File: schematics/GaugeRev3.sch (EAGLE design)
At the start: 35 parts, among them U1 ARDUINO_MINI, U2 VID29, U3 FT232RL-BASICSSOP

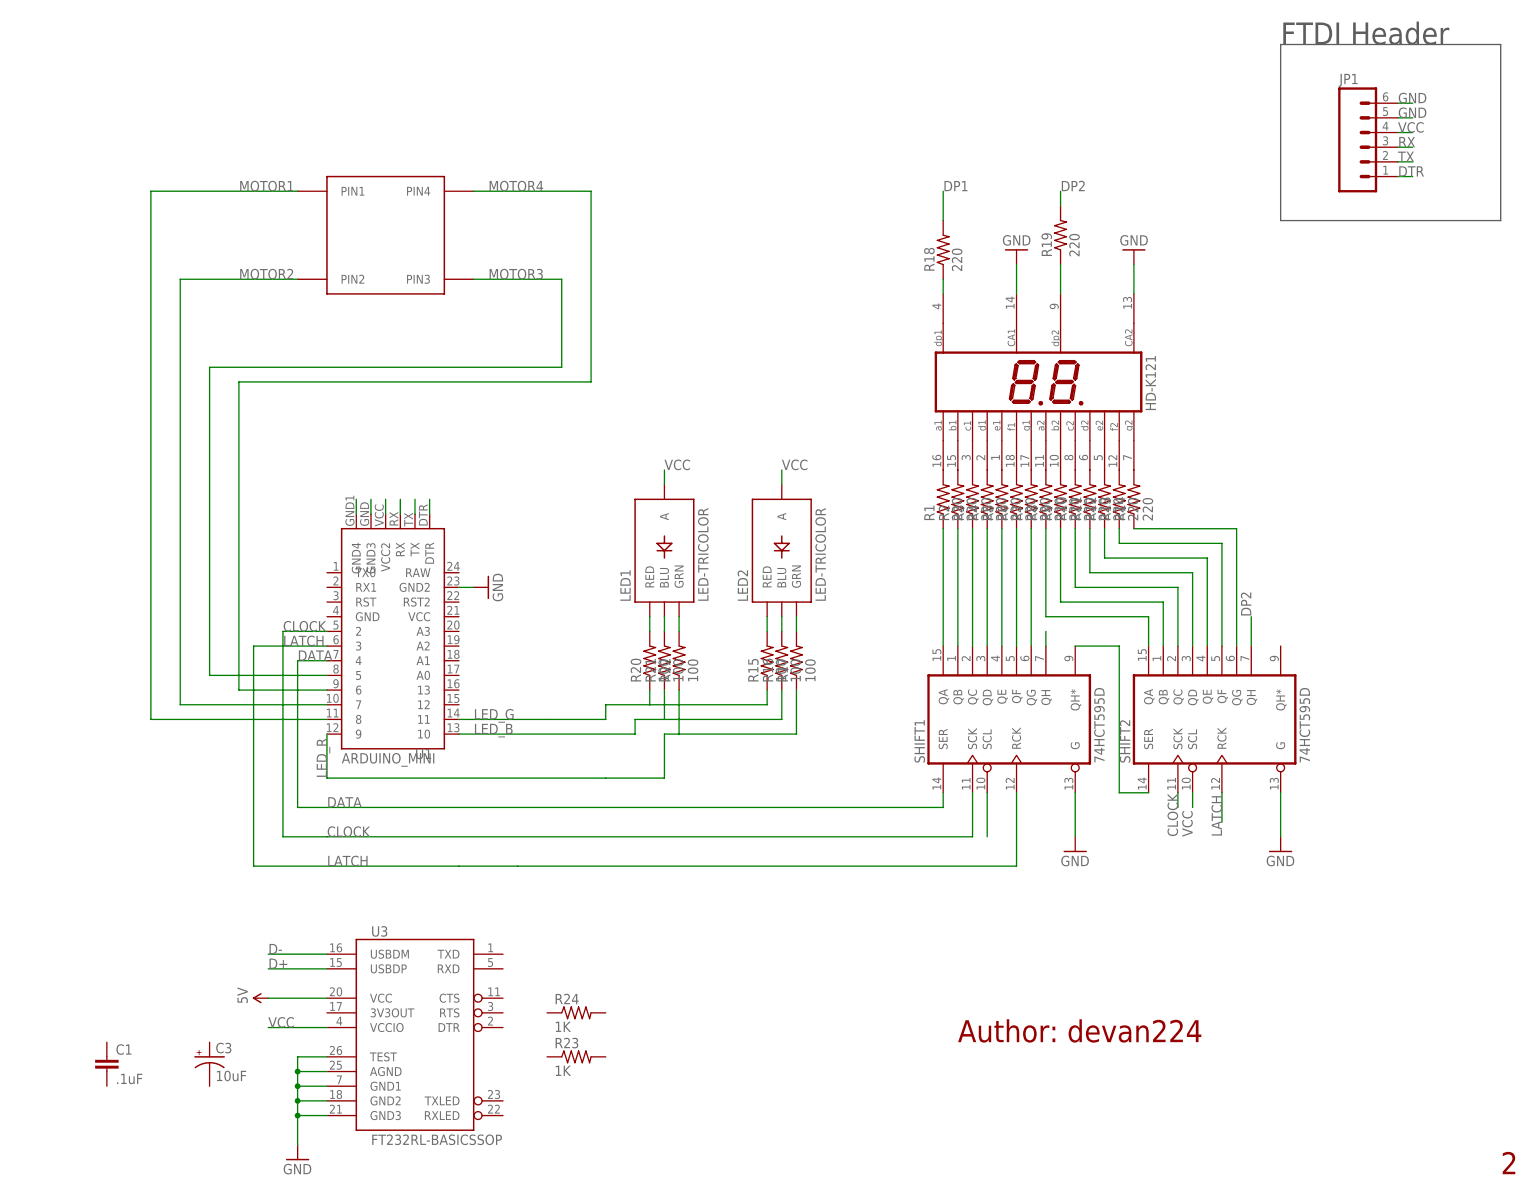
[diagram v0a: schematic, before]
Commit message: updated schematics
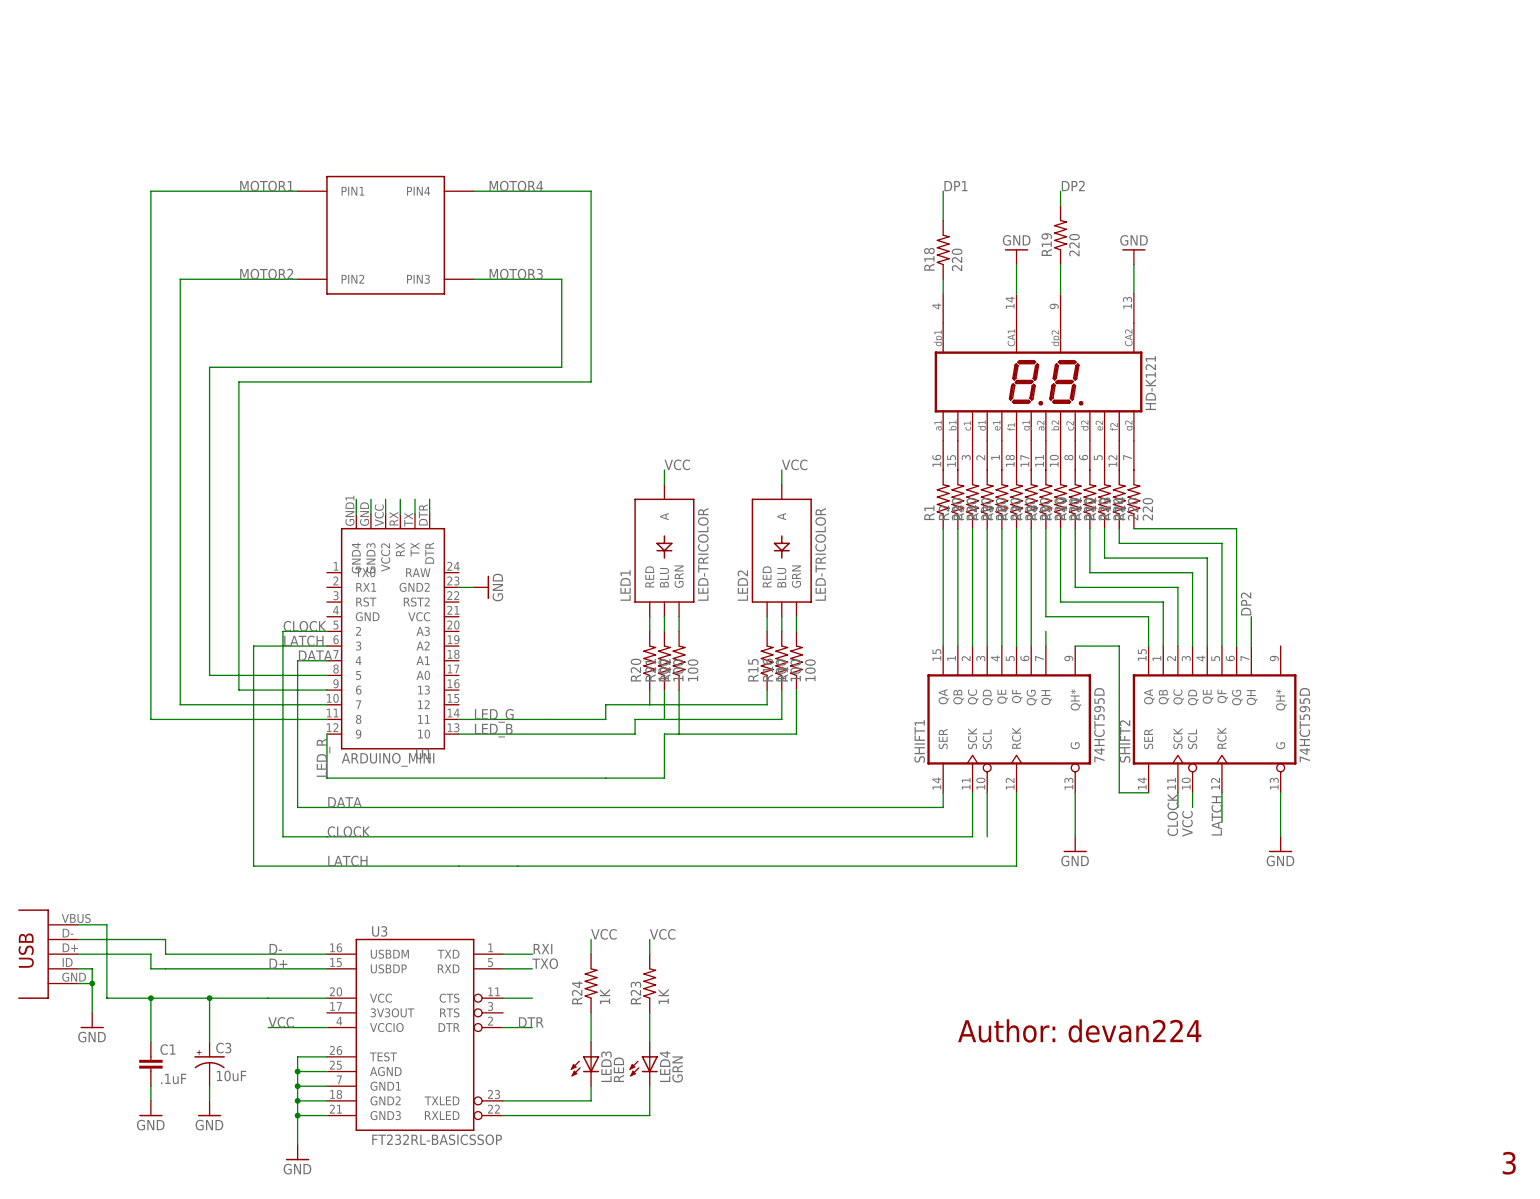
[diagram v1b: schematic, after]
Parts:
- removed JP1: (no value), SparkFun:M06SIP
- added LED3: RED, SparkFun:LED1206
- added LED4: GRN, SparkFun:LED1206
- added U$1: USB-MINI-VERT, Evans:USB-MINI-VERT
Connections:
- removed net 5V: U3.VCC
- removed net RX: JP1.3, U1.RX
- removed net TX: JP1.2, U1.TX
- new net N$17: LED3.C, U3.TXLED
- new net N$18: LED4.C, U3.RXLED
- new net N$27: LED4.A, R23.1
- new net N$28: LED3.A, R24.1
- new net RXI: U1.RX, U3.TXD
- new net TXO: U1.TX, U3.RXD
- new net VBUS: C1.1, C3.+, U$1.VBUS, U3.VCC
- net D+: now also U$1.D+
- net D-: now also U$1.D-
- net DTR: now also U3.DTR; no longer JP1.1
- net GND: now also C1.2, C3.-, U$1.GND, U$1.ID, U3.CTS; no longer JP1.5, JP1.6
- net VCC: now also R23.2, R24.2; no longer JP1.4
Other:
- note added: "3"
- note removed: "2"
- note removed: "FTDI Header"
- moved on the sheet: C1, R23, R24
